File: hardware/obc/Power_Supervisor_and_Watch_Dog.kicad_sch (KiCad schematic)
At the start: 23 parts, among them Q103 IRF7306, Q105 PMBT2222A, Q106 MBT2222ADW1T1, Q107 MBT2222ADW1T1

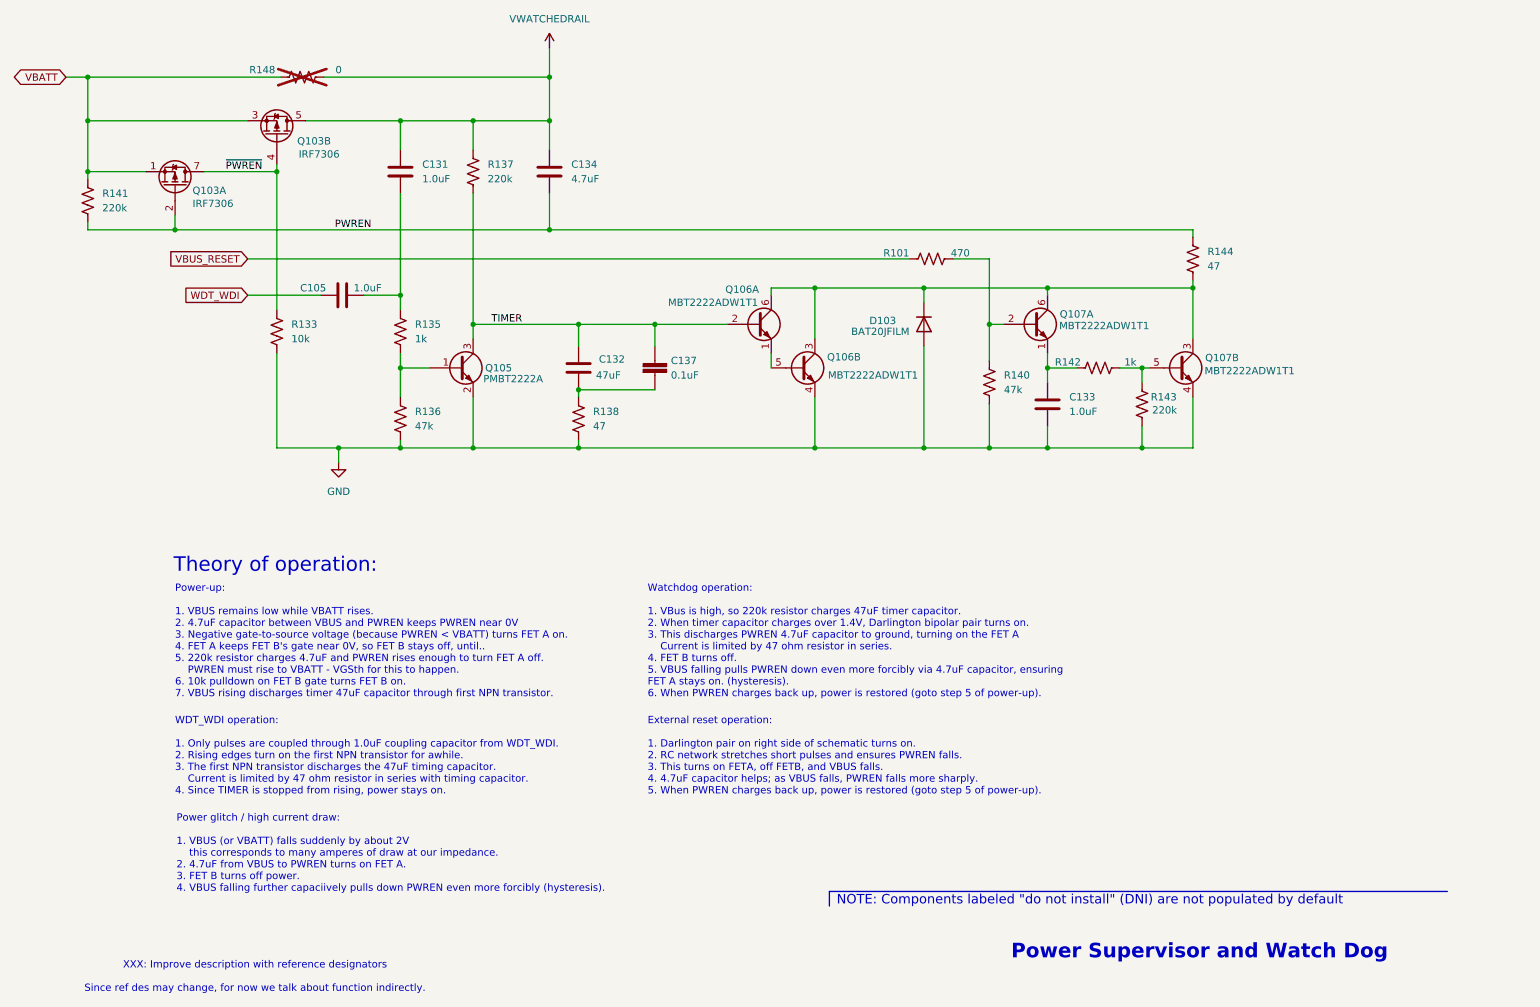
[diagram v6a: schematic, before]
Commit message: obc: refactors and renumbers
- renumber pages for more logical review order
- renumber reference designators to get smaller numbers
- small changes to layout from early design review
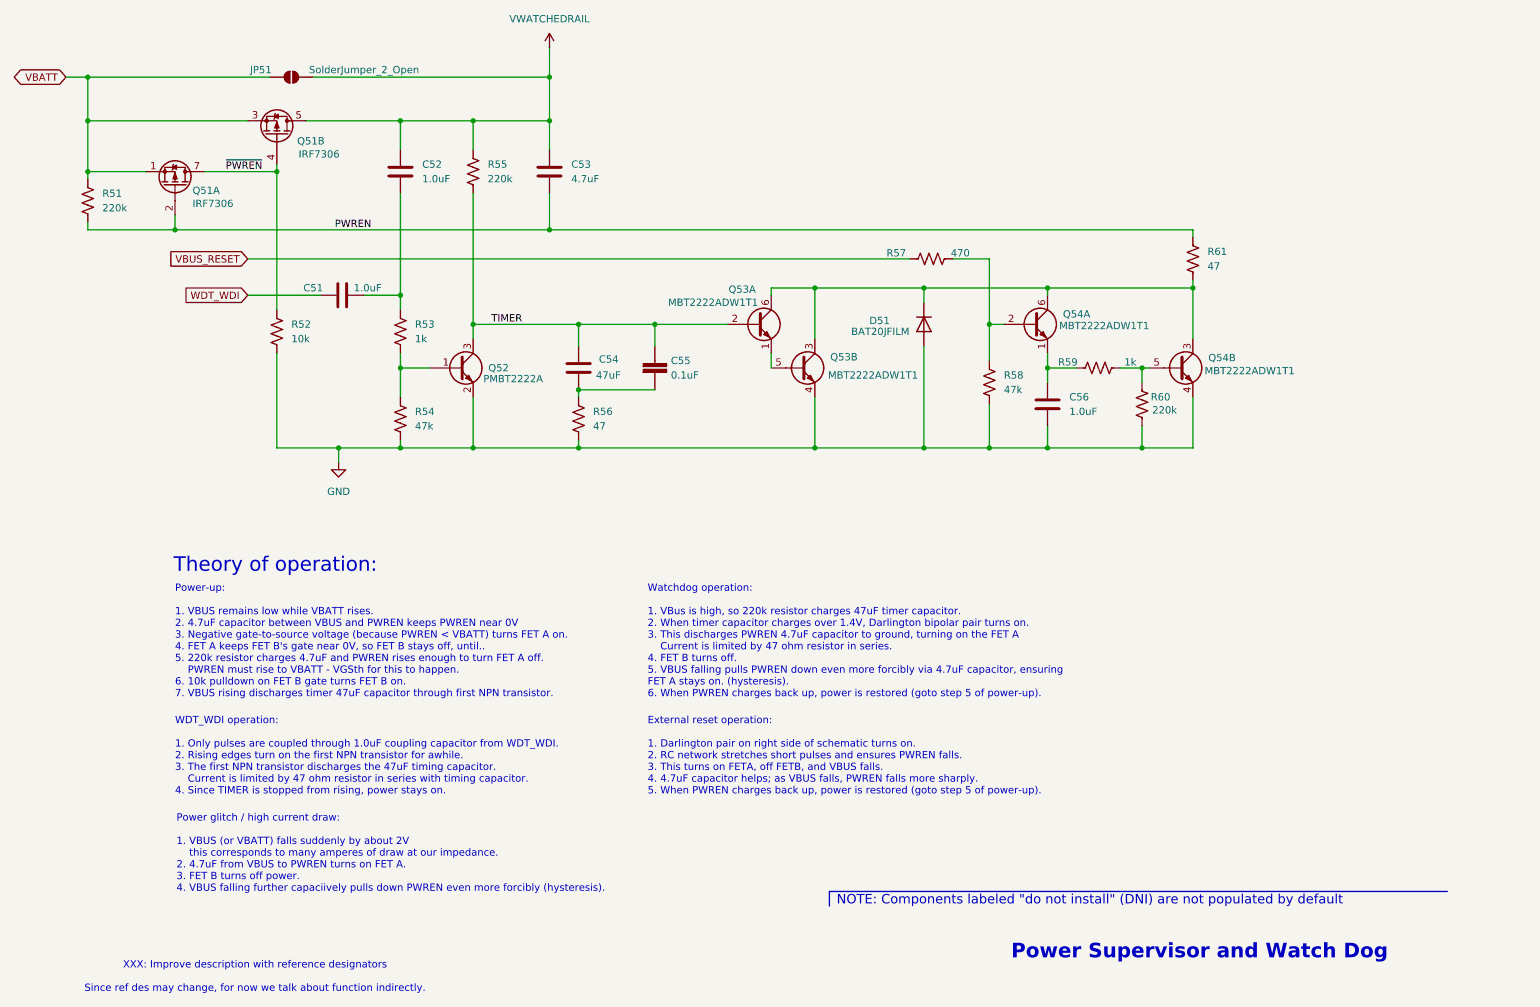
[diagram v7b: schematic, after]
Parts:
- removed R148: 0, Resistor_SMD:R_0603_1608Metric, symbol Device:R_US
- added JP51: SolderJumper_2_Open, Jumper:SolderJumper-2_P1.3mm_Open_TrianglePad1.0x1.5mm, symbol Jumper:SolderJumper_2_Open
- renumbered C105 to C51, C131 to C52, C134 to C53, C132 to C54, C137 to C55, C133 to C56, D103 to D51, Q103 to Q51, Q105 to Q52, Q106 to Q53, Q107 to Q54, R141 to R51, R133 to R52, R135 to R53, R136 to R54, R137 to R55, R138 to R56, R101 to R57, R140 to R58, R142 to R59, R143 to R60, R144 to R61
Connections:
- net VBATT: now also JP51.1 (A)
- net VWATCHEDRAIL: now also JP51.2 (B)

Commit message: obc: rename power nets for sanity
We've been confused by this for too long.

GNDREF -> PACKNEG
VCHRG -> PACKPOS
VBATT -> VRAIL
VBATT_SENSE -> INH_POS

Also add an OBC power subsystem diagram.
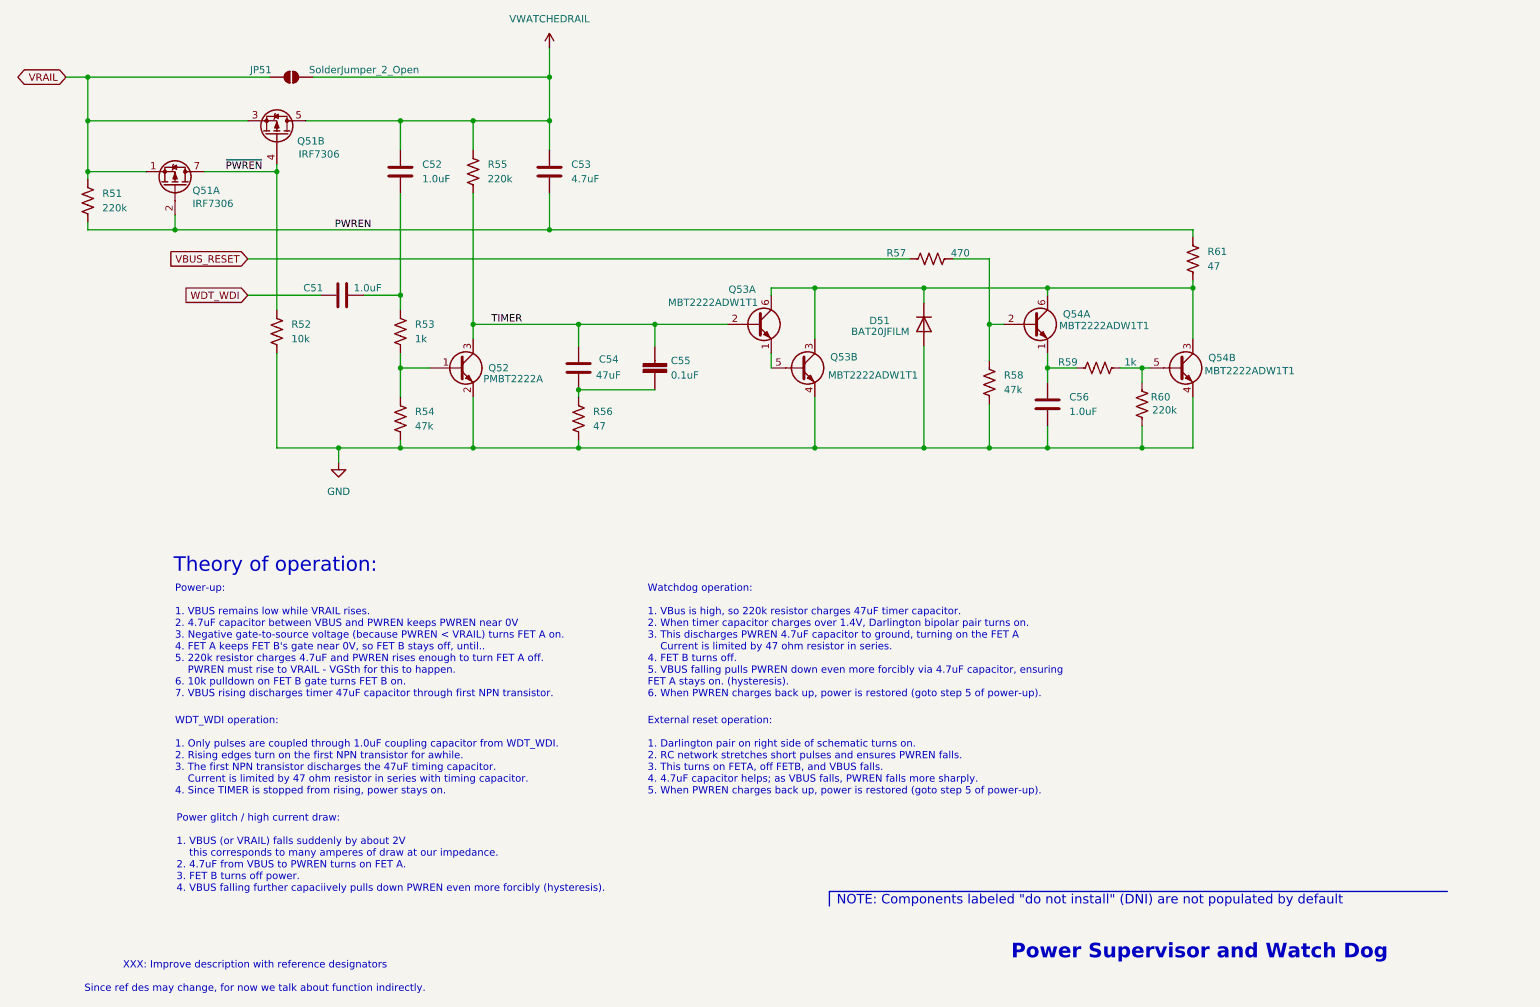
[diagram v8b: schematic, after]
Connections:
- net VBATT renamed VRAIL
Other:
- note added: "Power glitch / high current draw: 1. VBUS (or VRAIL) falls suddenly by about 2V this corresponds to many amperes of draw at our impedance. 2. 4.7uF from VBUS to PWREN turns on FET A. 3. FET B turns off power. 4. VBUS falling further capaciively pulls down PWREN even more forcibly (hysteresis)."
- note added: "Power-up: 1. VBUS remains low while VRAIL rises. 2. 4.7uF capacitor between VBUS and PWREN keeps PWREN near 0V 3. Negative gate-to-source voltage (because PWREN < VRAIL) turns FET A on. 4. FET A keeps FET B's gate near 0V, so FET B stays off, until.. 5. 220k resistor charges 4.7uF and PWREN rises enough to turn FET A off. PWREN must rise to VRAIL - VGSth for this to happen. 6. 10k pulldown on FET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"
- note removed: "Power glitch / high current draw: 1. VBUS (or VBATT) falls suddenly by about 2V this corresponds to many amperes of draw at our impedance. 2. 4.7uF from VBUS to PWREN turns on FET A. 3. FET B turns off power. 4. VBUS falling further capaciively pulls down PWREN even more forcibly (hysteresis)."
- note removed: "Power-up: 1. VBUS remains low while VBATT rises. 2. 4.7uF capacitor between VBUS and PWREN keeps PWREN near 0V 3. Negative gate-to-source voltage (because PWREN < VBATT) turns FET A on. 4. FET A keeps FET B's gate near 0V, so FET B stays off, until.. 5. 220k resistor charges 4.7uF and PWREN rises enough to turn FET A off. PWREN must rise to VBATT - VGSth for this to happen. 6. 10k pulldown on FET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"
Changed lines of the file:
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@@
 		)
 	)
-	(text "Power glitch / high current draw:\n\n1. VBUS (or VBATT) falls suddenly by about 2V\n	this corresponds to many amperes of draw at our impedance.\n2. 4.7uF from VBUS to PWREN turns on FET A.\n3. FET B turns off power.\n4. VBUS falling further capaciively pulls down PWREN even more forcibly (hysteresis)."
+	(text "Power glitch / high current draw:\n\n1. VBUS (or VRAIL) falls suddenly by about 2V\n	this corresponds to many amperes of draw at our impedance.\n2. 4.7uF from VBUS to PWREN turns on FET A.\n3. FET B turns off power.\n4. VBUS falling further capaciively pulls down PWREN even more forcibly (hysteresis)."
 		(exclude_from_sim no)
 		(at 44.704 155.448 0)
@@
 		)
 	)
-	(text "Power-up:\n\n1. VBUS remains low while VBATT rises.\n2. 4.7uF capacitor between VBUS and PWREN keeps PWREN near 0V\n3. Negative gate-to-source voltage (because PWREN < VBATT) turns FET A on.\n4. FET A keeps FET B's gate near 0V, so FET B stays off, until..\n5. 220k resistor charges 4.7uF and PWREN rises enough to turn FET A off.\n	PWREN must rise to VBATT - VGSth for this to happen.\n6. 10k pulldown on FET B gate turns FET B on.\n7. VBUS rising discharges timer 47uF capacitor through first NPN transistor."
+	(text "Power-up:\n\n1. VBUS remains low while VRAIL rises.\n2. 4.7uF capacitor between VBUS and PWREN keeps PWREN near 0V\n3. Negative gate-to-source voltage (because PWREN < VRAIL) turns FET A on.\n4. FET A keeps FET B's gate near 0V, so FET B stays off, until..\n5. 220k resistor charges 4.7uF and PWREN rises enough to turn FET A off.\n	PWREN must rise to VRAIL - VGSth for this to happen.\n6. 10k pulldown on FET B gate turns FET B on.\n7. VBUS rising discharges timer 47uF capacitor through first NPN transistor."
 		(exclude_from_sim no)
 		(at 44.45 115.316 0)
@@
 		)
 	)
-	(global_label "VBATT"
+	(global_label "VRAIL"
 		(shape bidirectional)
 		(at 25.4 26.67 180)
